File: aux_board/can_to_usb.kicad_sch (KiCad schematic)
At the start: 14 parts, among them SW1 EVP-AA602W, SW2 EVP-AA602W, U1 STM32L496RGT6

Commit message: inching toward ordering SCI and AUX
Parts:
- added J5, J6: Conn_01x05_Pin, Connector_PinHeader_2.54mm:PinHeader_1x05_P2.54mm_Vertical, symbol Connector:Conn_01x05_Pin
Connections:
- net 3V3: now also J5.4 (Pin_4), J6.4 (Pin_4)
- net 5V: now also J5.5 (Pin_5), J6.5 (Pin_5)
- net GND: now also J5.1 (Pin_1), J6.1 (Pin_1)
- net UART4_TX: now reaches U1.51 (PC10)
- net UART4_TX: now also J5.3 (Pin_3)
- net UART4_RX: now reaches U1.52 (PC11)
- net UART4_RX: now also J5.2 (Pin_2)
- net UART5_TX: now reaches U1.53 (PC12)
- net UART5_TX: now also J6.3 (Pin_3)
- net UART5_RX: now reaches U1.54 (PD2)
- net UART5_RX: now also J6.2 (Pin_2)
- no-connect marks 20 -> 16

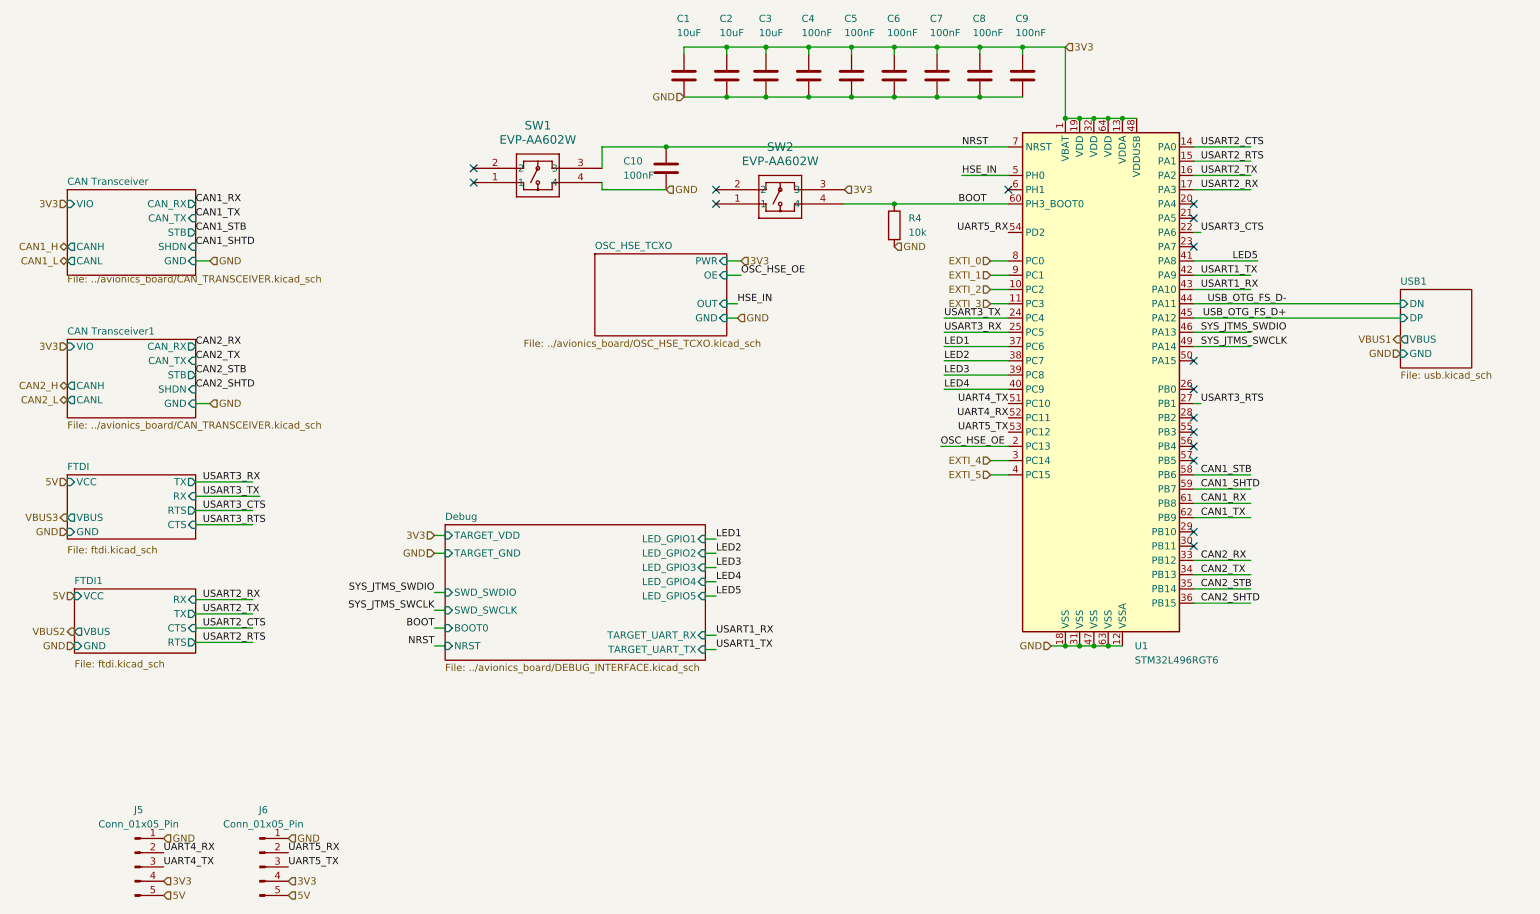
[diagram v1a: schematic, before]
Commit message: tweaking SCI and AUX for production, using common sheets as much as possible
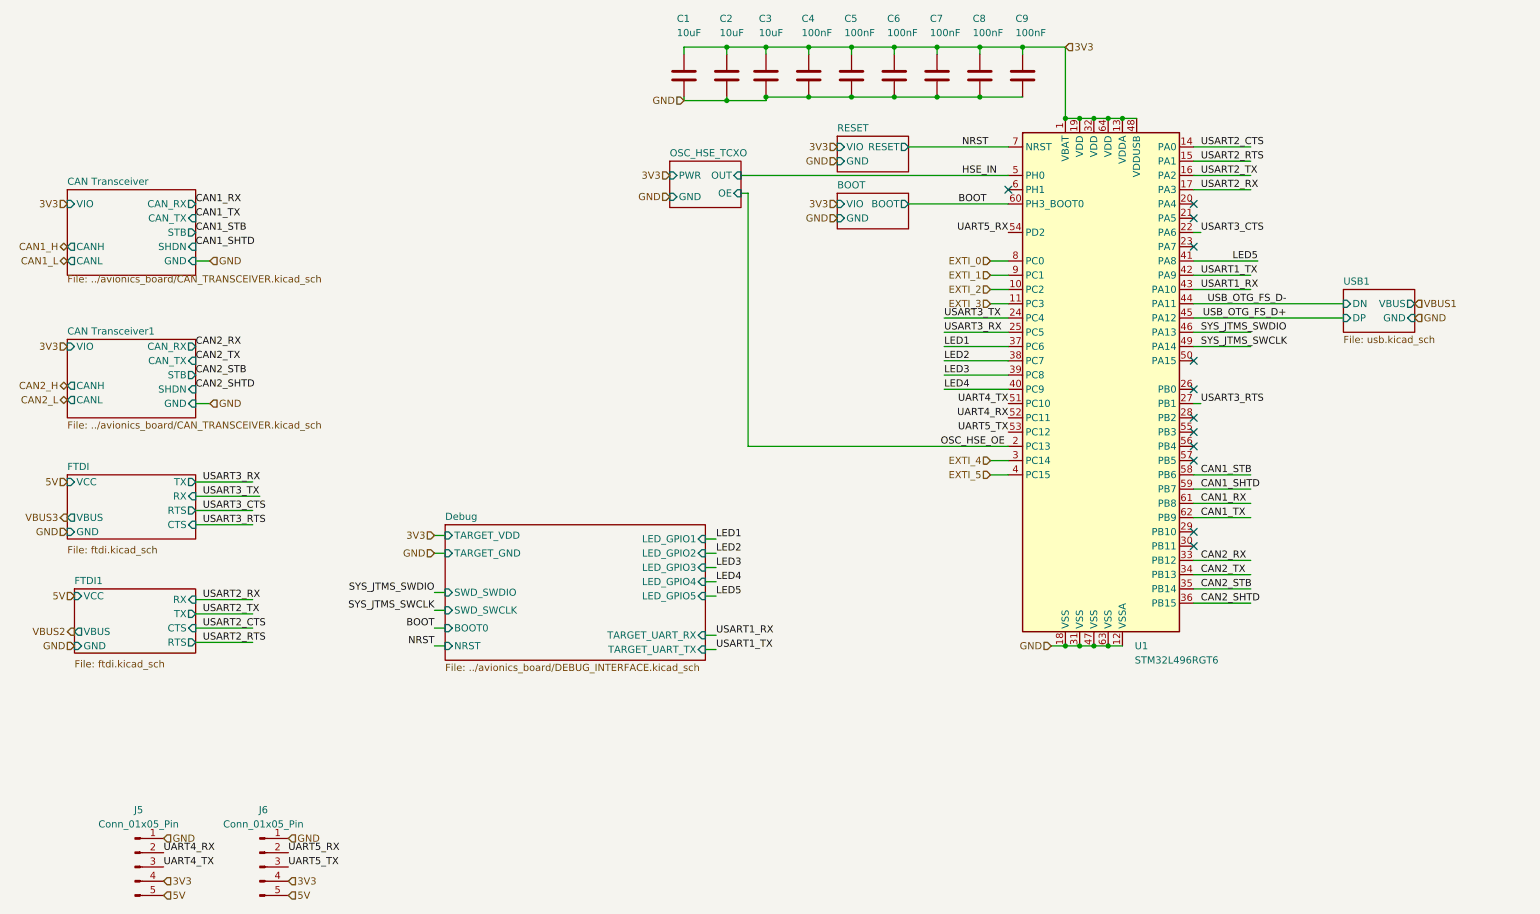
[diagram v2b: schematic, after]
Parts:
- removed C10: 100nF, Capacitor_SMD:C_0402_1005Metric_Pad0.74x0.62mm_HandSolder, symbol Device:C
- removed R4: 10k, Resistor_SMD:R_0603_1608Metric_Pad0.98x0.95mm_HandSolder, symbol Device:R
- removed SW1, SW2: EVP-AA602W, Project:EVP602AA, symbol Project:EVP-AA602W
- U1: symbol Project:STM32L496RGTx -> Common:STM32L496RGTx
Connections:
- no-connect marks 16 -> 12
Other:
- added sheet BOOT (../avionics_board/boot.kicad_sch)
- added sheet RESET (../sci_board/reset.kicad_sch)

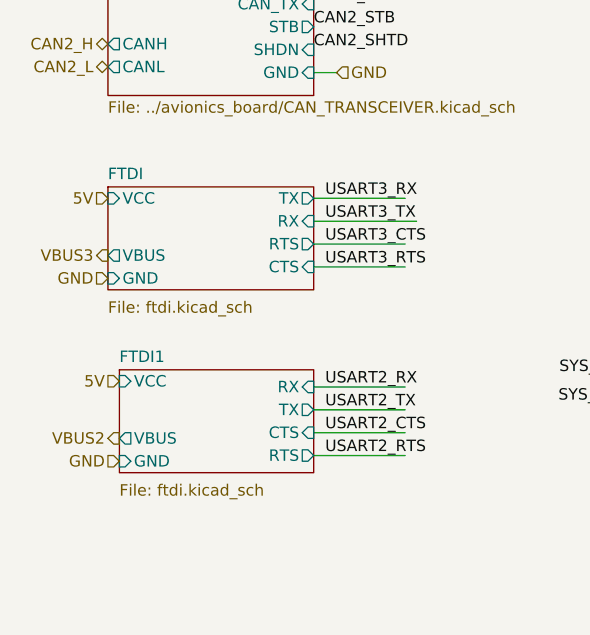
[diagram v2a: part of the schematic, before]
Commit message: clenup BOM for SCI and AUX
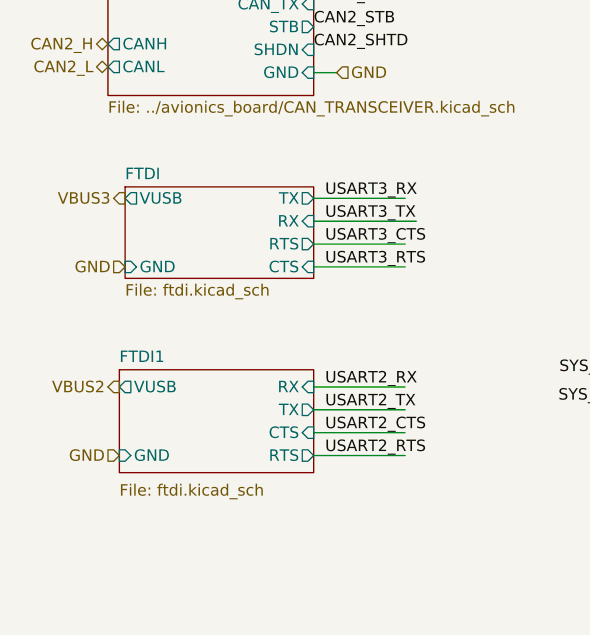
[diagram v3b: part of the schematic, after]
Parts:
- J5, J6: Manufacturer (none) -> generic; Part Number (none) -> generic
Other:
- sheet FTDI ports: added VUSB; removed VBUS, VCC
- sheet FTDI1 ports: added VUSB; removed VBUS, VCC

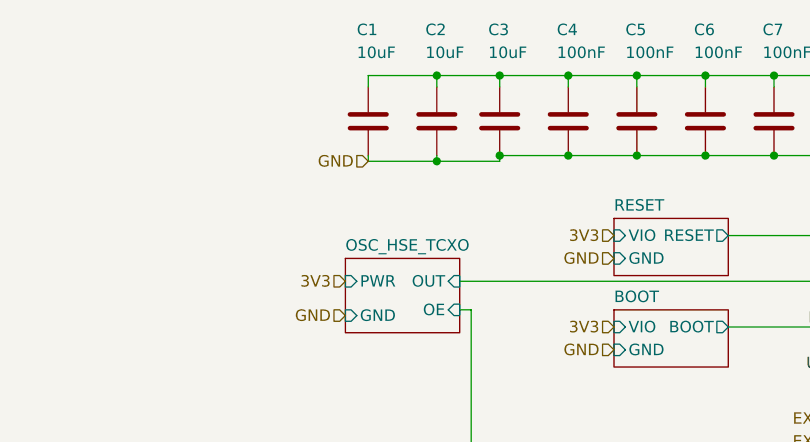
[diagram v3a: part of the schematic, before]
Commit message: cleaning up bom: remove main camera port since it has not pullups and capacitors, correcting some errors in camera switch
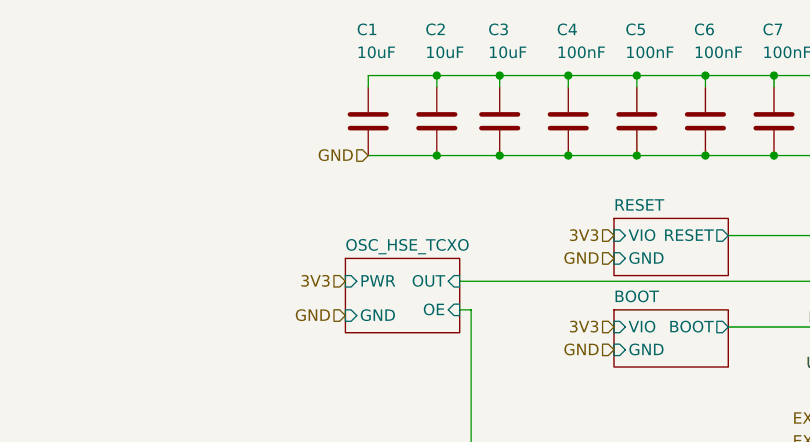
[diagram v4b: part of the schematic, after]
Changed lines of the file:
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@@
-	)
-	(junction
-		(at 142.875 45.085)
-		(diameter 0)
-		(color 0 0 0 0)
 	)
 	(junction
@@
 	)
 	(junction
+		(at 142.875 44.45)
+		(diameter 0)
+		(color 0 0 0 0)
+	)
+	(junction
 		(at 172.72 35.56)
 		(diameter 0)
@@
 	(wire
 		(pts
-			(xy 149.86 45.085) (xy 149.86 44.45)
-		)
-		(stroke
-			(width 0)
-			(type default)
-		)
-	)
-	(wire
-		(pts
 			(xy 200.66 142.24) (xy 203.2 142.24)
 		)
@@
 	(wire
 		(pts
-			(xy 135.255 45.085) (xy 142.875 45.085)
+			(xy 135.255 44.45) (xy 142.875 44.45)
 		)
 		(stroke
@@
 	(wire
 		(pts
-			(xy 142.875 45.085) (xy 142.875 44.45)
-		)
-		(stroke
-			(width 0)
-			(type default)
-		)
-	)
-	(wire
-		(pts
 			(xy 195.58 35.56) (xy 203.2 35.56)
 		)
@@
 	(wire
 		(pts
-			(xy 135.255 45.085) (xy 135.255 44.45)
-		)
-		(stroke
-			(width 0)
-			(type default)
-		)
-	)
-	(wire
-		(pts
-			(xy 142.875 45.085) (xy 149.86 45.085)
+			(xy 142.875 44.45) (xy 149.86 44.45)
 		)
 		(stroke
@@
 	(hierarchical_label "GND"
 		(shape input)
-		(at 135.255 45.085 180)
-		(fields_autoplaced yes)
-		(effects
+		(at 135.255 44.45 180)
+		(fields_autoplaced yes)
+		(effects
